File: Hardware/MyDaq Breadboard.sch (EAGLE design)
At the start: 12 parts, among them U1 BREADBOARDCLEAR

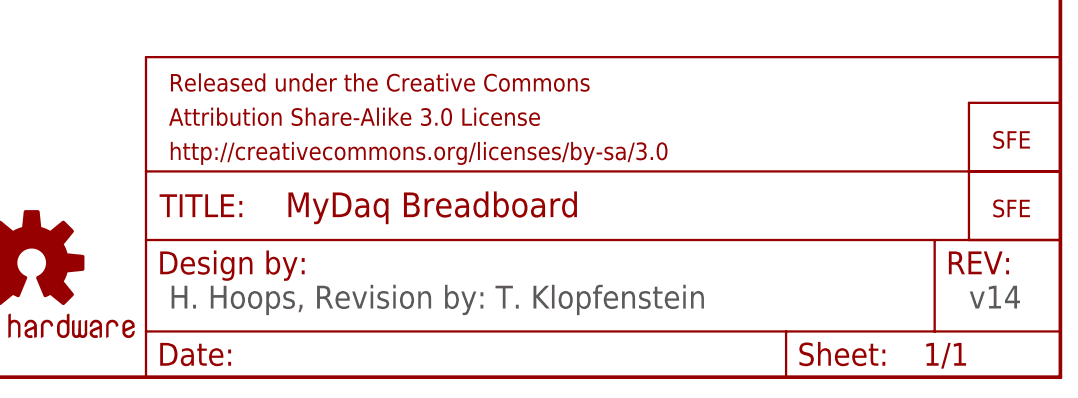
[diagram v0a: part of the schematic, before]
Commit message: Centered logos and changed revision to symbol
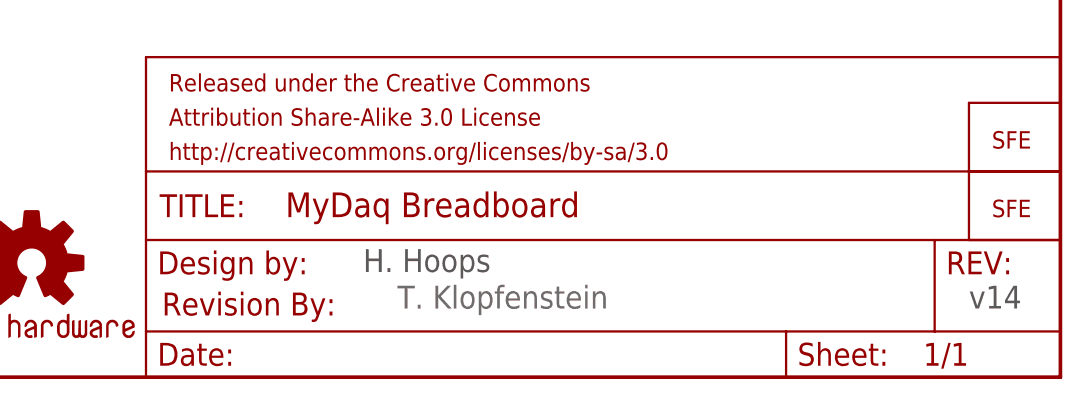
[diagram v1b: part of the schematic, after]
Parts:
- added U$3: REVISION, SparkFun-Aesthetics:REVISION
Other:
- note added: "H. Hoops"
- note added: "T. Klopfenstein"
- note removed: "H. Hoops, Revision by: T. Klopfenstein"
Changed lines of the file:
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@@
 <grid distance="0.1" unitdist="inch" unit="inch" style="lines" multiple="1" display="no" altdistance="0.01" altunitdist="inch" altunit="inch"/>
 <layers>
-<layer number="1" name="Top" color="4" fill="1" visible="yes" active="no"/>
-<layer number="2" name="Route2" color="1" fill="3" visible="yes" active="no"/>
-<layer number="3" name="Route3" color="4" fill="3" visible="yes" active="no"/>
-<layer number="4" name="Route4" color="1" fill="4" visible="yes" active="no"/>
-<layer number="5" name="Route5" color="4" fill="4" visible="yes" active="no"/>
-<layer number="6" name="Route6" color="1" fill="8" visible="yes" active="no"/>
-<layer number="7" name="Route7" color="4" fill="8" visible="yes" active="no"/>
-<layer number="8" name="Route8" color="1" fill="2" visible="yes" active="no"/>
-<layer number="9" name="Route9" color="4" fill="2" visible="yes" active="no"/>
-<layer number="10" name="Route10" color="1" fill="7" visible="yes" active="no"/>
-<layer number="11" name="Route11" color="4" fill="7" visible="yes" active="no"/>
-<layer number="12" name="Route12" color="1" fill="5" visible="yes" active="no"/>
-<layer number="13" name="Route13" color="4" fill="5" visible="yes" active="no"/>
-<layer number="14" name="Route14" color="1" fill="6" visible="yes" active="no"/>
-<layer number="15" name="Route15" color="4" fill="6" visible="yes" active="no"/>
-<layer number="16" name="Bottom" color="1" fill="1" visible="yes" active="no"/>
-<layer number="17" name="Pads" color="2" fill="1" visible="yes" active="no"/>
-<layer number="18" name="Vias" color="2" fill="1" visible="yes" active="no"/>
-<layer number="19" name="Unrouted" color="6" fill="1" visible="yes" active="no"/>
-<layer number="20" name="Dimension" color="15" fill="1" visible="yes" active="no"/>
-<layer number="21" name="tPlace" color="16" fill="1" visible="yes" active="no"/>
-<layer number="22" name="bPlace" color="14" fill="1" visible="yes" active="no"/>
-<layer number="23" name="tOrigins" color="15" fill="1" visible="yes" active="no"/>
-<layer number="24" name="bOrigins" color="15" fill="1" visible="yes" active="no"/>
-<layer number="25" name="tNames" color="7" fill="1" visible="yes" active="no"/>
-<layer number="26" name="bNames" color="7" fill="1" visible="yes" active="no"/>
-<layer number="27" name="tValues" color="7" fill="1" visible="yes" active="no"/>
-<layer number="28" name="bValues" color="7" fill="1" visible="yes" active="no"/>
+<layer number="1" name="Top" color="4" fill="1" visible="no" active="no"/>
+<layer number="2" name="Route2" color="1" fill="3" visible="no" active="no"/>
+<layer number="3" name="Route3" color="4" fill="3" visible="no" active="no"/>
+<layer number="4" name="Route4" color="1" fill="4" visible="no" active="no"/>
+<layer number="5" name="Route5" color="4" fill="4" visible="no" active="no"/>
+<layer number="6" name="Route6" color="1" fill="8" visible="no" active="no"/>
+<layer number="7" name="Route7" color="4" fill="8" visible="no" active="no"/>
+<layer number="8" name="Route8" color="1" fill="2" visible="no" active="no"/>
+<layer number="9" name="Route9" color="4" fill="2" visible="no" active="no"/>
+<layer number="10" name="Route10" color="1" fill="7" visible="no" active="no"/>
+<layer number="11" name="Route11" color="4" fill="7" visible="no" active="no"/>
+<layer number="12" name="Route12" color="1" fill="5" visible="no" active="no"/>
+<layer number="13" name="Route13" color="4" fill="5" visible="no" active="no"/>
+<layer number="14" name="Route14" color="1" fill="6" visible="no" active="no"/>
+<layer number="15" name="Route15" color="4" fill="6" visible="no" active="no"/>
+<layer number="16" name="Bottom" color="1" fill="1" visible="no" active="no"/>
+<layer number="17" name="Pads" color="2" fill="1" visible="no" active="no"/>
+<layer number="18" name="Vias" color="2" fill="1" visible="no" active="no"/>
+<layer number="19" name="Unrouted" color="6" fill="1" visible="no" active="no"/>
+<layer number="20" name="Dimension" color="15" fill="1" visible="no" active="no"/>
+<layer number="21" name="tPlace" color="16" fill="1" visible="no" active="no"/>
+<layer number="22" name="bPlace" color="14" fill="1" visible="no" active="no"/>
+<layer number="23" name="tOrigins" color="15" fill="1" visible="no" active="no"/>
+<layer number="24" name="bOrigins" color="15" fill="1" visible="no" active="no"/>
+<layer number="25" name="tNames" color="7" fill="1" visible="no" active="no"/>
+<layer number="26" name="bNames" color="7" fill="1" visible="no" active="no"/>
+<layer number="27" name="tValues" color="7" fill="1" visible="no" active="no"/>
+<layer number="28" name="bValues" color="7" fill="1" visible="no" active="no"/>
 <layer number="29" name="tStop" color="7" fill="3" visible="no" active="no"/>
 <layer number="30" name="bStop" color="7" fill="6" visible="no" active="no"/>
@@
 <layer number="35" name="tGlue" color="7" fill="4" visible="no" active="no"/>
 <layer number="36" name="bGlue" color="7" fill="5" visible="no" active="no"/>
-<layer number="37" name="tTest" color="7" fill="1" visible="yes" active="no"/>
-<layer number="38" name="bTest" color="7" fill="1" visible="yes" active="no"/>
+<layer number="37" name="tTest" color="7" fill="1" visible="no" active="no"/>
+<layer number="38" name="bTest" color="7" fill="1" visible="no" active="no"/>
 <layer number="39" name="tKeepout" color="4" fill="11" visible="no" active="no"/>
 <layer number="40" name="bKeepout" color="1" fill="11" visible="no" active="no"/>
@@
 <layer number="44" name="Drills" color="7" fill="1" visible="no" active="no"/>
 <layer number="45" name="Holes" color="7" fill="1" visible="no" active="no"/>
-<layer number="46" name="Milling" color="3" fill="1" visible="yes" active="no"/>
-<layer number="47" name="Measures" color="7" fill="1" visible="yes" active="no"/>
-<layer number="48" name="Document" color="7" fill="1" visible="yes" active="no"/>
-<layer number="49" name="Reference" color="7" fill="1" visible="yes" active="no"/>
-<layer number="50" name="dxf" color="7" fill="1" visible="yes" active="no"/>
-<layer number="51" name="tDocu" color="6" fill="1" visible="yes" active="no"/>
-<layer number="52" name="bDocu" color="7" fill="1" visible="yes" active="no"/>
-<layer number="53" name="tGND_GNDA" color="7" fill="9" visible="yes" active="no"/>
-<layer number="54" name="bGND_GNDA" color="1" fill="9" visible="yes" active="no"/>
-<layer number="56" name="wert" color="7" fill="1" visible="yes" active="no"/>
+<layer number="46" name="Milling" color="3" fill="1" visible="no" active="no"/>
+<layer number="47" name="Measures" color="7" fill="1" visible="no" active="no"/>
+<layer number="48" name="Document" color="7" fill="1" visible="no" active="no"/>
+<layer number="49" name="Reference" color="7" fill="1" visible="no" active="no"/>
+<layer number="50" name="dxf" color="7" fill="1" visible="no" active="no"/>
+<layer number="51" name="tDocu" color="6" fill="1" visible="no" active="no"/>
+<layer number="52" name="bDocu" color="7" fill="1" visible="no" active="no"/>
+<layer number="53" name="tGND_GNDA" color="7" fill="9" visible="no" active="no"/>
+<layer number="54" name="bGND_GNDA" color="1" fill="9" visible="no" active="no"/>
+<layer number="56" name="wert" color="7" fill="1" visible="no" active="no"/>
 <layer number="91" name="Nets" color="2" fill="1" visible="yes" active="yes"/>
 <layer number="92" name="Busses" color="1" fill="1" visible="yes" active="yes"/>
@@
 <part name="LOGO1" library="SparkFun-Aesthetics" deviceset="OSHW-LOGO" device="L"/>
 <part name="LOGO2" library="SparkFun-Aesthetics" deviceset="LOGO-SFE" device="SK"/>
+<part name="U$3" library="SparkFun-Aesthetics" deviceset="REVISION" device=""/>
 </parts>
 <sheets>
 <sheet>
 <plain>
-<text x="149.86" y="7.62" size="2.54" layer="97">H. Hoops, Revision by: T. Klopfenstein</text>
+<text x="171.45" y="11.684" size="2.54" layer="97">H. Hoops</text>
 <text x="238.76" y="7.62" size="2.54" layer="97">v14</text>
+<text x="175.26" y="7.62" size="2.54" layer="95">T. Klopfenstein</text>
 </plain>
 <instances>
@@
 <instance part="LOGO1" gate="G$1" x="134.62" y="12.7"/>
 <instance part="LOGO2" gate="G$1" x="241.3" y="17.78"/>
+<instance part="U$3" gate="G$1" x="149.098" y="6.858"/>
 </instances>
 <busses>
